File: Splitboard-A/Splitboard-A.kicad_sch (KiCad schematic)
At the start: 96 parts, among them J1 USB_C_Receptacle, J2 USB_C_Receptacle_USB2.0, K1 KEYSW, K10 KEYSW, K11 KEYSW, K12 KEYSW, K13 KEYSW, K14 KEYSW, K15 KEYSW, K16 KEYSW, K17 KEYSW, K18 KEYSW, K19 KEYSW, K2 KEYSW, K20 KEYSW, K21 KEYSW, K22 KEYSW, K23 KEYSW, K24 KEYSW, K25 KEYSW, K26 KEYSW, K27 KEYSW, K28 KEYSW, K29 KEYSW, K3 KEYSW, K30 KEYSW, K31 KEYSW, K32 KEYSW, K33 KEYSW, K34 KEYSW, K35 KEYSW, K36 KEYSW, K37 KEYSW, K38 KEYSW, K4 KEYSW, K5 KEYSW, K6 KEYSW, K7 KEYSW, K8 KEYSW, K9 KEYSW, SW1 RotaryEncoder, U1 STM32F407VGTx, U2 AMS1117-3.3, U3 CR2013-MI2120

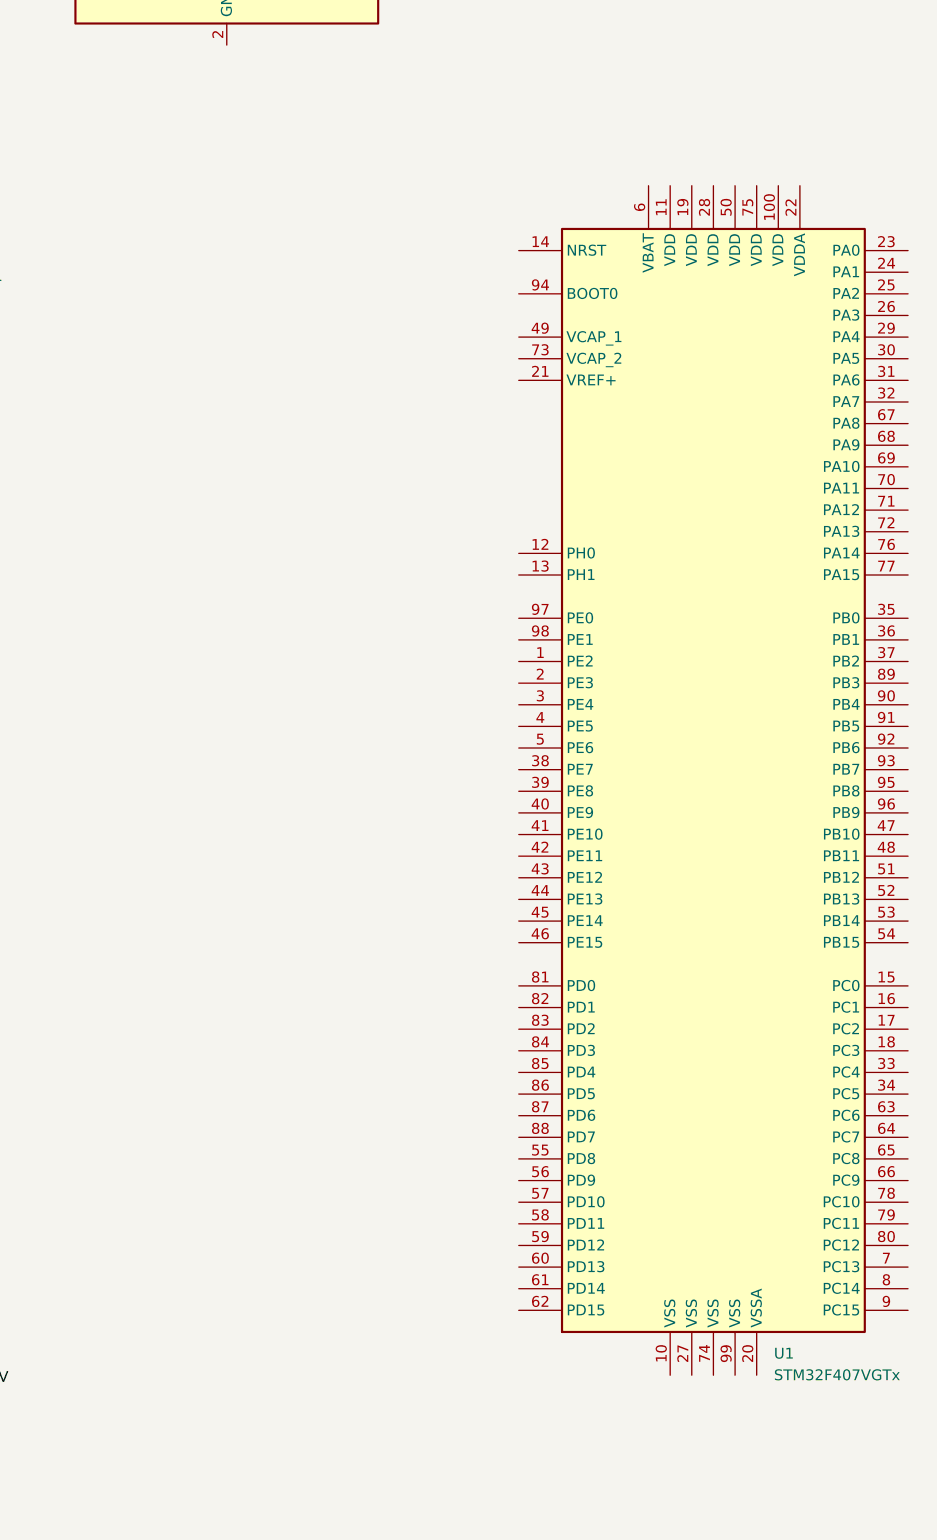
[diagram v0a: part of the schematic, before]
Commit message: Keyboard changes (added split to other half, component footprints)
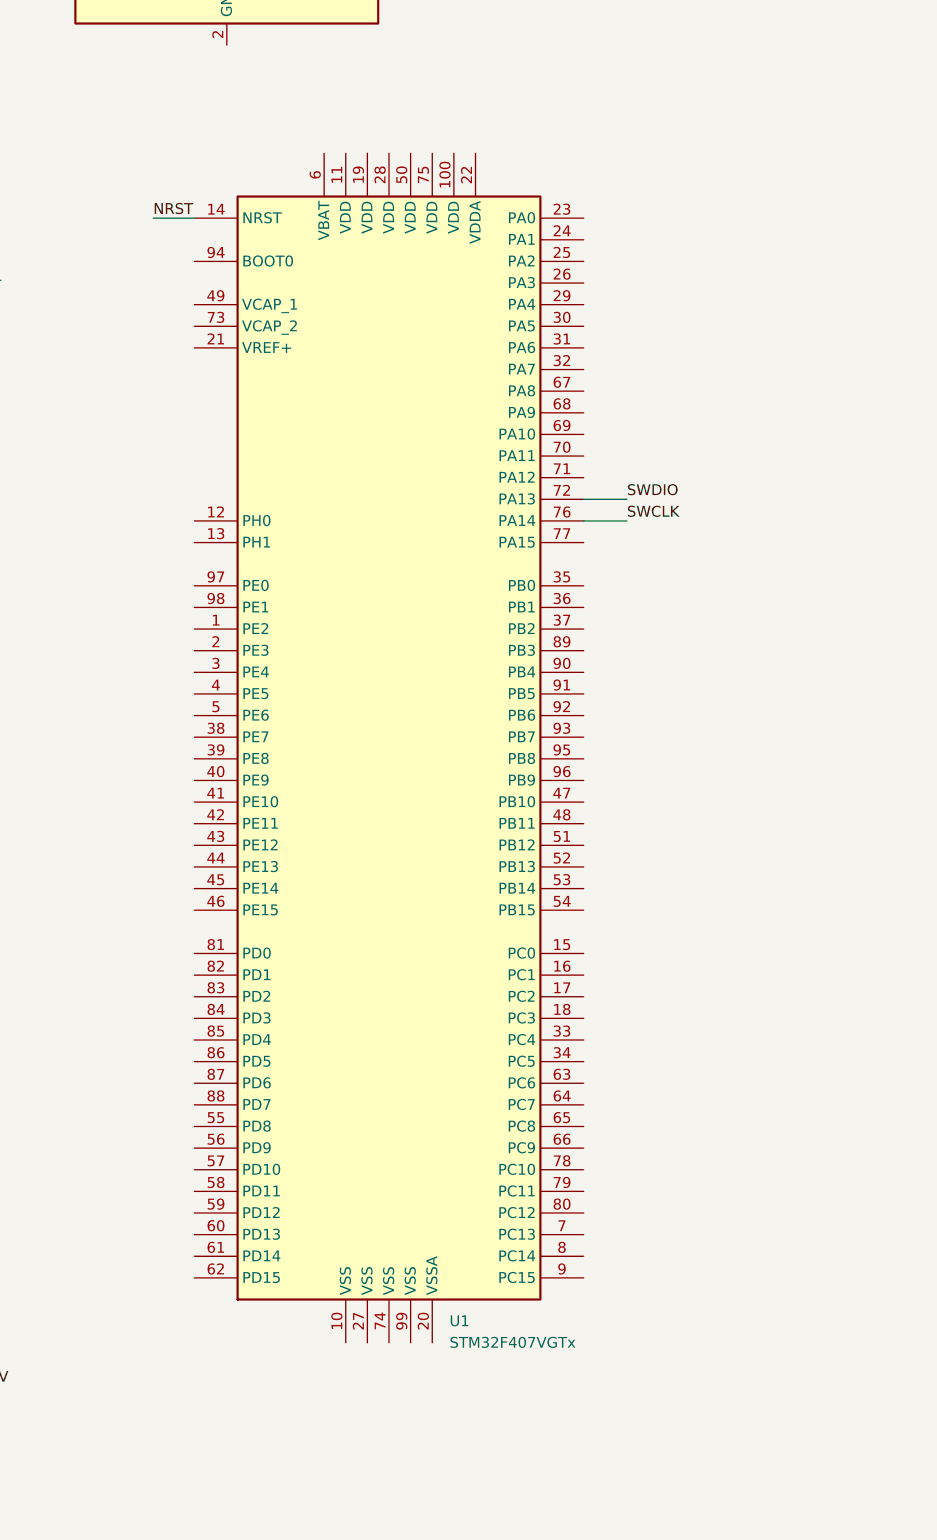
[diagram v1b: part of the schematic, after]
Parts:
- D39, D40, D41: footprint (none) -> Diode_SMD:D_SOD-123
- F1: footprint (none) -> Fuse:Fuse_BelFuse_0ZRE0125FF_L21.2mm_W5.3mm
- FB1: footprint (none) -> Resistor_SMD:R_0805_2012Metric
- J1, J2: footprint Connector_USB:USB_C_Receptacle_Amphenol_12401548E4-2A_CircularHoles -> USB_C_Receptacle_GCT_USB4085
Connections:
- net NRST: now reaches U1.14 (NRST)
- net SWDIO: now reaches U1.72 (PA13)
- net SWCLK: now reaches U1.76 (PA14)
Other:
- moved on the sheet: U1
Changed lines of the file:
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@@
+    (stroke (width 0) (type default) (color 0 0 0 0))
+  )
+  (wire (pts (xy 327.66 119.38) (xy 332.74 119.38))
     (stroke (width 0) (type default) (color 0 0 0 0))
   )
@@
     (stroke (width 0) (type default) (color 0 0 0 0))
   )
+  (wire (pts (xy 327.66 121.92) (xy 332.74 121.92))
+    (stroke (width 0) (type default) (color 0 0 0 0))
+  )
   (wire (pts (xy 153.67 81.28) (xy 153.67 82.55))
     (stroke (width 0) (type default) (color 0 0 0 0))
@@
   )
   (wire (pts (xy 101.6 260.35) (xy 101.6 264.16))
+    (stroke (width 0) (type default) (color 0 0 0 0))
+  )
+  (wire (pts (xy 277.114 86.36) (xy 281.94 86.36))
     (stroke (width 0) (type default) (color 0 0 0 0))
   )
@@
     (effects (font (size 1.27 1.27)) (justify right bottom))
   )
+  (label "SWCLK" (at 332.74 121.92 0)
+    (effects (font (size 1.27 1.27)) (justify left bottom))
+  )
   (label "col1" (at 102.87 33.02 0)
     (effects (font (size 1.27 1.27)) (justify left bottom))
   )
+  (label "NRST" (at 277.114 86.36 0)
+    (effects (font (size 1.27 1.27)) (justify left bottom))
+  )
   (label "col3" (at 147.32 33.02 0)
     (effects (font (size 1.27 1.27)) (justify left bottom))
@@
   )
   (label "col2" (at 125.73 33.02 0)
+    (effects (font (size 1.27 1.27)) (justify left bottom))
+  )
+  (label "SWDIO" (at 332.74 119.38 0)
     (effects (font (size 1.27 1.27)) (justify left bottom))
   )
@@
     (property "Reference" "J2" (id 0) (at 236.22 215.9 0))
     (property "Value" "USB_C_Receptacle_USB2.0" (id 1) (at 236.22 218.44 0))
-    (property "Footprint" "Connector_USB:USB_C_Receptacle_Amphenol_12401548E4-2A_CircularHoles" (id 2) (at 240.03 238.76 0)
+    (property "Footprint" "USB_C_Receptacle_GCT_USB4085" (id 2) (at 240.03 238.76 0)
       (effects (font (size 1.27 1.27)) hide)
     )
@@
     (property "Reference" "F1" (id 0) (at 88.9 199.39 90))
     (property "Value" "500mA" (id 1) (at 88.9 201.93 90))
-    (property "Footprint" "" (id 2) (at 88.9 207.518 90)
+    (property "Footprint" "Fuse:Fuse_BelFuse_0ZRE0125FF_L21.2mm_W5.3mm" (id 2) (at 88.9 207.518 90)
       (effects (font (size 1.27 1.27)) hide)
     )
@@
     (property "Reference" "D39" (id 0) (at 75.2475 199.39 0))
     (property "Value" "D_Schottky" (id 1) (at 75.2475 201.93 0))
-    (property "Footprint" "" (id 2) (at 74.93 205.74 0)
+    (property "Footprint" "Diode_SMD:D_SOD-123" (id 2) (at 74.93 205.74 0)
       (effects (font (size 1.27 1.27)) hide)
     )
@@
       (effects (font (size 1.27 1.27)) (justify left))
     )
-    (property "Footprint" "" (id 2) (at 101.6 246.38 0)
+    (property "Footprint" "Diode_SMD:D_SOD-123" (id 2) (at 101.6 246.38 0)
       (effects (font (size 1.27 1.27)) hide)
     )
@@
     )
   )
-  (symbol (lib_id "MCU_ST_STM32F4:STM32F407VGTx") (at 342.9 151.13 0) (unit 1)
+  (symbol (lib_id "MCU_ST_STM32F4:STM32F407VGTx") (at 304.8 147.32 0) (unit 1)
     (in_bom yes) (on_board yes) (fields_autoplaced)
-    (property "Reference" "U1" (id 0) (at 349.9994 219.71 0)
-      (effects (font (size 1.27 1.27)) (justify left))
-    )
-    (property "Value" "STM32F407VGTx" (id 1) (at 349.9994 222.25 0)
-      (effects (font (size 1.27 1.27)) (justify left))
-    )
-    (property "Footprint" "Package_QFP:LQFP-100_14x14mm_P0.5mm" (id 2) (at 325.12 217.17 0)
+    (property "Reference" "U1" (id 0) (at 311.8994 215.9 0)
+      (effects (font (size 1.27 1.27)) (justify left))
+    )
+    (property "Value" "STM32F407VGTx" (id 1) (at 311.8994 218.44 0)
+      (effects (font (size 1.27 1.27)) (justify left))
+    )
+    (property "Footprint" "Package_QFP:LQFP-100_14x14mm_P0.5mm" (id 2) (at 287.02 213.36 0)
       (effects (font (size 1.27 1.27)) (justify right) hide)
     )
-    (property "Datasheet" "http://www.st.com/st-web-ui/static/active/en/resource/technical/document/datasheet/DM00037051.pdf" (id 3) (at 342.9 151.13 0)
+    (property "Datasheet" "http://www.st.com/st-web-ui/static/active/en/resource/technical/document/datasheet/DM00037051.pdf" (id 3) (at 304.8 147.32 0)
       (effects (font (size 1.27 1.27)) hide)
     )
@@
       (effects (font (size 1.27 1.27)) (justify left))
     )
-    (property "Footprint" "" (id 2) (at 101.6 256.54 0)
+    (property "Footprint" "Diode_SMD:D_SOD-123" (id 2) (at 101.6 256.54 0)
       (effects (font (size 1.27 1.27)) hide)
     )
@@
     (property "Reference" "J1" (id 0) (at 236.22 121.92 0))
     (property "Value" "USB_C_Receptacle" (id 1) (at 236.22 124.46 0))
-    (property "Footprint" "Connector_USB:USB_C_Receptacle_Amphenol_12401548E4-2A_CircularHoles" (id 2) (at 240.03 154.94 0)
+    (property "Footprint" "USB_C_Receptacle_GCT_USB4085" (id 2) (at 240.03 154.94 0)
       (effects (font (size 1.27 1.27)) hide)
     )
@@
     (property "Reference" "FB1" (id 0) (at 102.8192 198.12 90))
     (property "Value" "100 @ 100 MHz" (id 1) (at 102.8192 200.66 90))
-    (property "Footprint" "" (id 2) (at 102.87 207.518 90)
+    (property "Footprint" "Resistor_SMD:R_0805_2012Metric" (id 2) (at 102.87 207.518 90)
       (effects (font (size 1.27 1.27)) hide)
     )
@@
     )
     (path "/5ef3210e-de8e-444d-b7a3-c6a85e5c3868"
-      (reference "D39") (unit 1) (value "D_Schottky") (footprint "")
+      (reference "D39") (unit 1) (value "D_Schottky") (footprint "Diode_SMD:D_SOD-123")
     )
     (path "/72889ed1-e862-48e3-80ee-367de236f080"
-      (reference "D40") (unit 1) (value "D_Schottky") (footprint "")
+      (reference "D40") (unit 1) (value "D_Schottky") (footprint "Diode_SMD:D_SOD-123")
     )
     (path "/c277ec15-48fa-4ea5-9d5a-d78437114532"
-      (reference "D41") (unit 1) (value "D_Schottky") (footprint "")
+      (reference "D41") (unit 1) (value "D_Schottky") (footprint "Diode_SMD:D_SOD-123")
     )
     (path "/57f8246e-a191-4570-bfdf-f223a2bb82eb"
-      (reference "F1") (unit 1) (value "500mA") (footprint "")
+      (reference "F1") (unit 1) (value "500mA") (footprint "Fuse:Fuse_BelFuse_0ZRE0125FF_L21.2mm_W5.3mm")
     )
     (path "/f3cc7ab8-c40c-45a6-9789-37cfaf8bc1a0"
-      (reference "FB1") (unit 1) (value "100 @ 100 MHz") (footprint "")
+      (reference "FB1") (unit 1) (value "100 @ 100 MHz") (footprint "Resistor_SMD:R_0805_2012Metric")
     )
     (path "/02347b75-549f-4492-9e78-de5033b26b20"
@@
     )
     (path "/ca3e1f62-e8a9-4767-80e4-2c6ec5b2c287"
-      (reference "J1") (unit 1) (value "USB_C_Receptacle") (footprint "Connector_USB:USB_C_Receptacle_Amphenol_12401548E4-2A_CircularHoles")
+      (reference "J1") (unit 1) (value "USB_C_Receptacle") (footprint "USB_C_Receptacle_GCT_USB4085")
     )
     (path "/032f4b10-628a-44ba-9b33-02cf515cc703"
-      (reference "J2") (unit 1) (value "USB_C_Receptacle_USB2.0") (footprint "Connector_USB:USB_C_Receptacle_Amphenol_12401548E4-2A_CircularHoles")
+      (reference "J2") (unit 1) (value "USB_C_Receptacle_USB2.0") (footprint "USB_C_Receptacle_GCT_USB4085")
     )
     (path "/00000000-0000-0000-0000-00006051f173"

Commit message: Schematic modifications
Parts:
- added C1, C10, C11, C12, C13, C14, C5, C6, C7, C8, C9: 100nF, symbol Device:C
- added J3: Conn_01x04, symbol Connector_Generic:Conn_01x04
- added R1, R2: R, symbol Device:R
- added SW2: SW_Push, symbol Switch:SW_Push
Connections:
- net 5V is gone; now on net Vbus: J2.A4 (VBUS), J2.A9 (VBUS), J2.B4 (VBUS), J2.B9 (VBUS)
- net Voltage Regulator Input is gone; now on net Power Regulator: D39.2 (A)
- net +3v3 to micro: now also U1.100 (VDD), U1.11 (VDD), U1.19 (VDD), U1.28 (VDD), U1.50 (VDD), U1.75 (VDD), U3.1 (VCC), C10.1, C11.1, C12.1, C13.1, C14.1, C5.1, C6.1, C7.1, C8.1, C9.1, R1.1, R2.1
- net GND: now also J1.A1 (GND), J1.A12 (GND), J1.B1 (GND), J1.B12 (GND), J1.S1 (SHIELD), SW1.C, U1.10 (VSS), U1.27 (VSS), U1.74 (VSS), U1.99 (VSS), U3.2 (GND), C1.1, C10.2, C11.2, C12.2, C13.2, C14.2, C5.2, C6.2, C7.2, C8.2, C9.2, J3.1 (Pin_1), SW2.1
- net NRST: now also C1.2, J3.4 (Pin_4), SW2.2
- net SWCLK: now also J3.3 (Pin_3)
- net SWDIO: now also J3.2 (Pin_2)
- net col0: now also U1.88 (PD7)
- net col1: now also U1.55 (PD8)
- net col2: now also U1.56 (PD9)
- net col3: now also U1.57 (PD10)
- net col4: now also U1.58 (PD11)
- net col5: now also U1.59 (PD12)
- net row0: now also U1.81 (PD0)
- net row1: now also U1.82 (PD1)
- net row2: now also U1.83 (PD2)
- net row3: now also U1.84 (PD3)
- net row4: now also U1.85 (PD4)
- net row5: now also U1.86 (PD5)
- net row6: now also U1.87 (PD6)
- net USB_DP: now reaches J2.A6 (D+)
- net USB_DP: now also U1.71 (PA12)
- net USB_DM: now reaches J2.A7 (D-)
- net USB_DM: now also U1.70 (PA11)
- net at SW1.A: now also R1.2
- net at SW1.B: now also R2.2

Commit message: Schematic changes, linked both boards under a new project
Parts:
- removed C1: 100nF, symbol Device:C
- removed J3: Conn_01x04, symbol Connector_Generic:Conn_01x04
- added C4: 100nF, symbol Device:C
- added J3: Conn_01x07, symbol Connector_Generic:Conn_01x07
- renumbered C3 to C1, C4 to C3, D39 to D1, D7 to D10, D8 to D11, D9 to D12, D10 to D13, D11 to D14, D12 to D15, D13 to D16, D14 to D17, D15 to D18, D16 to D19, D40 to D2, D17 to D20, D18 to D21, D19 to D22, D20 to D23, D21 to D24, D22 to D25, D23 to D26, D24 to D27, D25 to D28, D26 to D29, D41 to D3, D27 to D30, D28 to D31, D29 to D32, D30 to D33, D31 to D34, D32 to D35, D33 to D36, D34 to D37, D35 to D38, D36 to D39, D1 to D4, D37 to D40, D38 to D41, D2 to D5, D3 to D6, D4 to D7, D5 to D8, D6 to D9, J2 to J1, J1 to J2, R3 to R1, R4 to R2, R1 to R3, R2 to R4, U2 to U1, U1 to U2
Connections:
- net +3.3V: now also C10.1, C11.1, C12.1, C13.1, C14.1, C5.1, C6.1, C7.1, C8.1, C9.1, J2.A4 (VBUS), J2.A9 (VBUS), J2.B4 (VBUS), J2.B9 (VBUS), R3.1, R4.1, U2.100 (VDD), U2.11 (VDD), U2.19 (VDD), U2.28 (VDD), U2.50 (VDD), U2.75 (VDD), U3.1 (VCC), J3.6 (Pin_6)
- net +3v3 to micro: now also R1.2, R2.2; no longer C10.1, C11.1, C12.1, C13.1, C14.1, C5.1, C6.1, C7.1, C8.1, C9.1, R3.1, R4.1, U2.100 (VDD), U2.11 (VDD), U2.19 (VDD), U2.28 (VDD), U2.50 (VDD), U2.75 (VDD), U3.1 (VCC)
- net GND: now also C4.1, J3.1 (Pin_1), J3.7 (Pin_7)
- net NRST: now also C4.2, J3.4 (Pin_4)
- net Power Regulator: no longer D1.2 (A)
- net SWCLK: now also J3.3 (Pin_3)
- net SWDIO: now also J3.2 (Pin_2)
- net ENC_B: now reaches R4.2, SW1.B
- net ENC_B: now also U2.61 (PD14)
- net ENC_A: now reaches R3.2, SW1.A
- net ENC_A: now also U2.60 (PD13)
- net CS: now reaches U3.3 (~{CS})
- net CS: now also J2.B10 (RX1-)
- net MOSI: now reaches U3.6 (MOSI)
- net MOSI: now also J2.B11 (RX1+)
- net SCK: now reaches U3.7 (SCK)
- net SCK: now also J2.A2 (TX1+)
- net MISO: now reaches U3.9 (MISO)
- net MISO: now also J2.A3 (TX1-)
- net SCL: now reaches J2.A10 (RX2-)
- net SDA: now reaches J2.A11 (RX2+)
- net Vbus renamed Voltage Regulator Input
- net Voltage Regulator Input: now also D1.2 (A); no longer R1.2, R2.2
- new net SWO: J3.5 (Pin_5)
- no-connect marks 0 -> 10
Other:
- note added: "Decoupling Capacitors"
- note added: "ESD Protection"
- note added: "Keyboard Matrix"
- note added: "LCD"
- note added: "Mounting Holes"
- note added: "Programming Header"
- note added: "Reset"
- note added: "Rotary Encoder"
- note added: "STM32F407"
- note added: "USB-C PC"
- note added: "USB-C Side B"
- note added: "Voltage Regulator"
- moved on the sheet: C1, C10, C11, C12, C13, C14, C2, C3, C5, C6, C7, C8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
